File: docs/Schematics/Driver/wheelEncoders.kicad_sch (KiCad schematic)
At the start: 6 parts

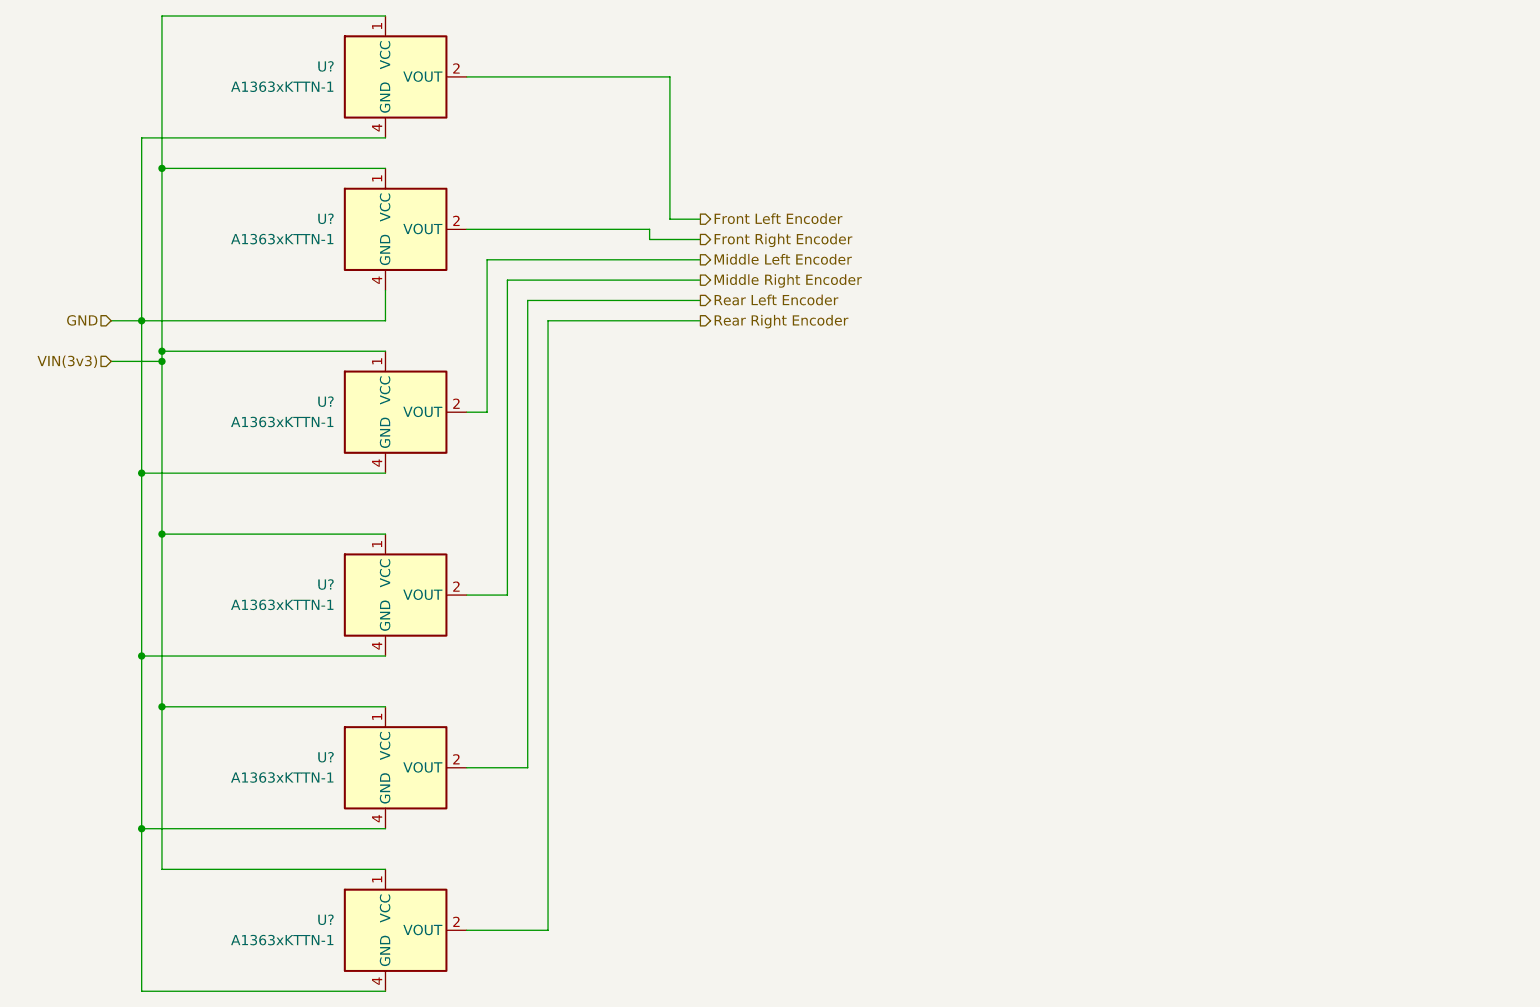
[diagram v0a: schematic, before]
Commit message: First scematic design for the card
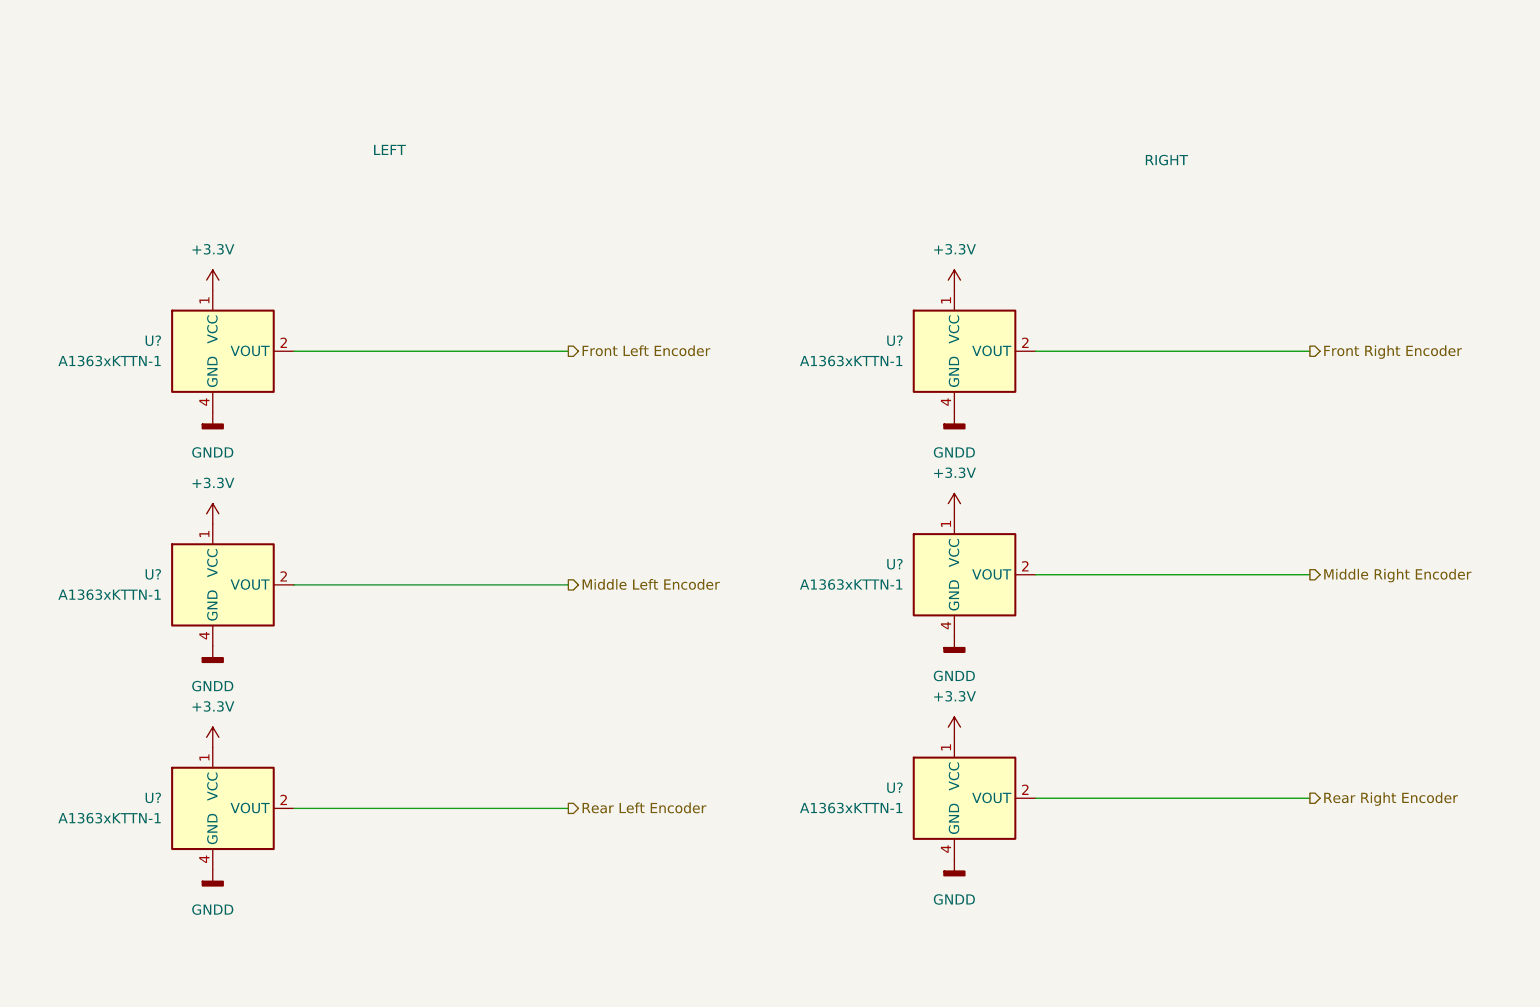
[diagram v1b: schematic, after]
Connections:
- net GND renamed GNDD
- net VIN(3v3) renamed +3.3V
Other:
- note added: "LEFT"
- note added: "RIGHT"
- company: (none) -> HiQ
- title: (none) -> Arty Z7 IO expander card
- moved on the sheet: U?

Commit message: Added footprints and a symbol for the level shifters
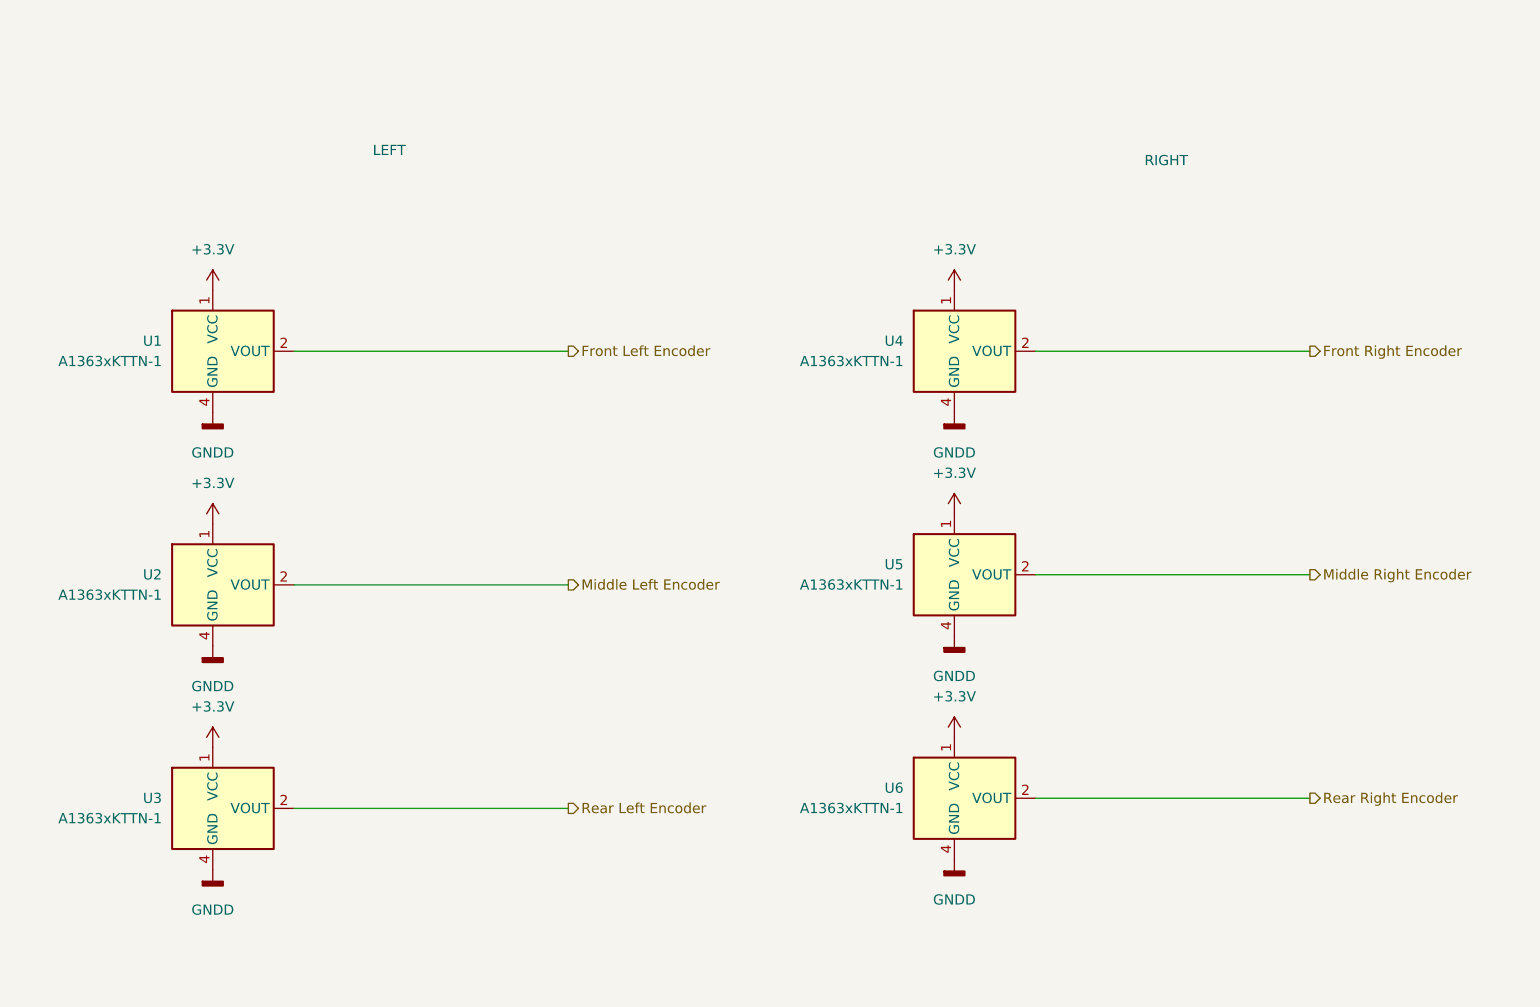
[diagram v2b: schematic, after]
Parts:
- gave numbers to parts that had none: 6
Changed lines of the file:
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@@
   (symbol (lib_id "Sensor_Current:A1363xKTTN-1") (at 87.63 92.71 0) (unit 1)
     (in_bom yes) (on_board yes) (fields_autoplaced)
-    (property "Reference" "U?" (id 0) (at 81.28 91.4399 0)
+    (property "Reference" "U2" (id 0) (at 81.28 91.4399 0)
       (effects (font (size 1.27 1.27)) (justify right))
     )
@@
   (symbol (lib_id "power:GNDD") (at 180.34 71.12 0) (unit 1)
     (in_bom yes) (on_board yes) (fields_autoplaced)
-    (property "Reference" "#PWR?" (id 0) (at 180.34 77.47 0)
+    (property "Reference" "#PWR043" (id 0) (at 180.34 77.47 0)
       (effects (font (size 1.27 1.27)) hide)
     )
@@
   (symbol (lib_id "power:GNDD") (at 87.63 100.33 0) (unit 1)
     (in_bom yes) (on_board yes) (fields_autoplaced)
-    (property "Reference" "#PWR?" (id 0) (at 87.63 106.68 0)
+    (property "Reference" "#PWR039" (id 0) (at 87.63 106.68 0)
       (effects (font (size 1.27 1.27)) hide)
     )
@@
   (symbol (lib_id "power:GNDD") (at 180.34 127 0) (unit 1)
     (in_bom yes) (on_board yes) (fields_autoplaced)
-    (property "Reference" "#PWR?" (id 0) (at 180.34 133.35 0)
+    (property "Reference" "#PWR047" (id 0) (at 180.34 133.35 0)
       (effects (font (size 1.27 1.27)) hide)
     )
@@
   (symbol (lib_id "Sensor_Current:A1363xKTTN-1") (at 87.63 120.65 0) (unit 1)
     (in_bom yes) (on_board yes) (fields_autoplaced)
-    (property "Reference" "U?" (id 0) (at 81.28 119.3799 0)
+    (property "Reference" "U3" (id 0) (at 81.28 119.3799 0)
       (effects (font (size 1.27 1.27)) (justify right))
     )
@@
   (symbol (lib_id "power:+3.3V") (at 87.63 113.03 0) (unit 1)
     (in_bom yes) (on_board yes) (fields_autoplaced)
-    (property "Reference" "#PWR?" (id 0) (at 87.63 116.84 0)
+    (property "Reference" "#PWR040" (id 0) (at 87.63 116.84 0)
       (effects (font (size 1.27 1.27)) hide)
     )
@@
   (symbol (lib_id "power:+3.3V") (at 87.63 55.88 0) (unit 1)
     (in_bom yes) (on_board yes) (fields_autoplaced)
-    (property "Reference" "#PWR?" (id 0) (at 87.63 59.69 0)
+    (property "Reference" "#PWR036" (id 0) (at 87.63 59.69 0)
       (effects (font (size 1.27 1.27)) hide)
     )
@@
   (symbol (lib_id "Sensor_Current:A1363xKTTN-1") (at 180.34 63.5 0) (unit 1)
     (in_bom yes) (on_board yes) (fields_autoplaced)
-    (property "Reference" "U?" (id 0) (at 173.99 62.2299 0)
+    (property "Reference" "U4" (id 0) (at 173.99 62.2299 0)
       (effects (font (size 1.27 1.27)) (justify right))
     )
@@
   (symbol (lib_id "power:+3.3V") (at 180.34 111.76 0) (unit 1)
     (in_bom yes) (on_board yes) (fields_autoplaced)
-    (property "Reference" "#PWR?" (id 0) (at 180.34 115.57 0)
+    (property "Reference" "#PWR046" (id 0) (at 180.34 115.57 0)
       (effects (font (size 1.27 1.27)) hide)
     )
@@
   (symbol (lib_id "power:+3.3V") (at 87.63 85.09 0) (unit 1)
     (in_bom yes) (on_board yes) (fields_autoplaced)
-    (property "Reference" "#PWR?" (id 0) (at 87.63 88.9 0)
+    (property "Reference" "#PWR038" (id 0) (at 87.63 88.9 0)
       (effects (font (size 1.27 1.27)) hide)
     )
@@
   (symbol (lib_id "power:GNDD") (at 180.34 99.06 0) (unit 1)
     (in_bom yes) (on_board yes) (fields_autoplaced)
-    (property "Reference" "#PWR?" (id 0) (at 180.34 105.41 0)
+    (property "Reference" "#PWR045" (id 0) (at 180.34 105.41 0)
       (effects (font (size 1.27 1.27)) hide)
     )
@@
   (symbol (lib_id "power:GNDD") (at 87.63 128.27 0) (unit 1)
     (in_bom yes) (on_board yes) (fields_autoplaced)
-    (property "Reference" "#PWR?" (id 0) (at 87.63 134.62 0)
+    (property "Reference" "#PWR041" (id 0) (at 87.63 134.62 0)
       (effects (font (size 1.27 1.27)) hide)
     )
@@
   (symbol (lib_id "Sensor_Current:A1363xKTTN-1") (at 87.63 63.5 0) (unit 1)
     (in_bom yes) (on_board yes) (fields_autoplaced)
-    (property "Reference" "U?" (id 0) (at 81.28 62.2299 0)
+    (property "Reference" "U1" (id 0) (at 81.28 62.2299 0)
       (effects (font (size 1.27 1.27)) (justify right))
     )
@@
   (symbol (lib_id "Sensor_Current:A1363xKTTN-1") (at 180.34 119.38 0) (unit 1)
     (in_bom yes) (on_board yes) (fields_autoplaced)
-    (property "Reference" "U?" (id 0) (at 173.99 118.1099 0)
+    (property "Reference" "U6" (id 0) (at 173.99 118.1099 0)
       (effects (font (size 1.27 1.27)) (justify right))
     )
@@
   (symbol (lib_id "power:+3.3V") (at 180.34 55.88 0) (unit 1)
     (in_bom yes) (on_board yes) (fields_autoplaced)
-    (property "Reference" "#PWR?" (id 0) (at 180.34 59.69 0)
+    (property "Reference" "#PWR042" (id 0) (at 180.34 59.69 0)
       (effects (font (size 1.27 1.27)) hide)
     )
@@
   (symbol (lib_id "power:+3.3V") (at 180.34 83.82 0) (unit 1)
     (in_bom yes) (on_board yes) (fields_autoplaced)
-    (property "Reference" "#PWR?" (id 0) (at 180.34 87.63 0)
+    (property "Reference" "#PWR044" (id 0) (at 180.34 87.63 0)
       (effects (font (size 1.27 1.27)) hide)
     )
@@
   (symbol (lib_id "power:GNDD") (at 87.63 71.12 0) (unit 1)
     (in_bom yes) (on_board yes) (fields_autoplaced)
-    (property "Reference" "#PWR?" (id 0) (at 87.63 77.47 0)
+    (property "Reference" "#PWR037" (id 0) (at 87.63 77.47 0)
       (effects (font (size 1.27 1.27)) hide)
     )
@@
   (symbol (lib_id "Sensor_Current:A1363xKTTN-1") (at 180.34 91.44 0) (unit 1)
     (in_bom yes) (on_board yes) (fields_autoplaced)
-    (property "Reference" "U?" (id 0) (at 173.99 90.1699 0)
-      (effects (font (size 1.27 1.27)) (justify right))
-    )
+    (property "Reference" "U5" (id 0) (at 173.99 90.1699 0)
+      (effects (font (size 1.27 1.27)) (justify right))
+    )

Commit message: Added caps and changed the connection from the motor sensors to plints
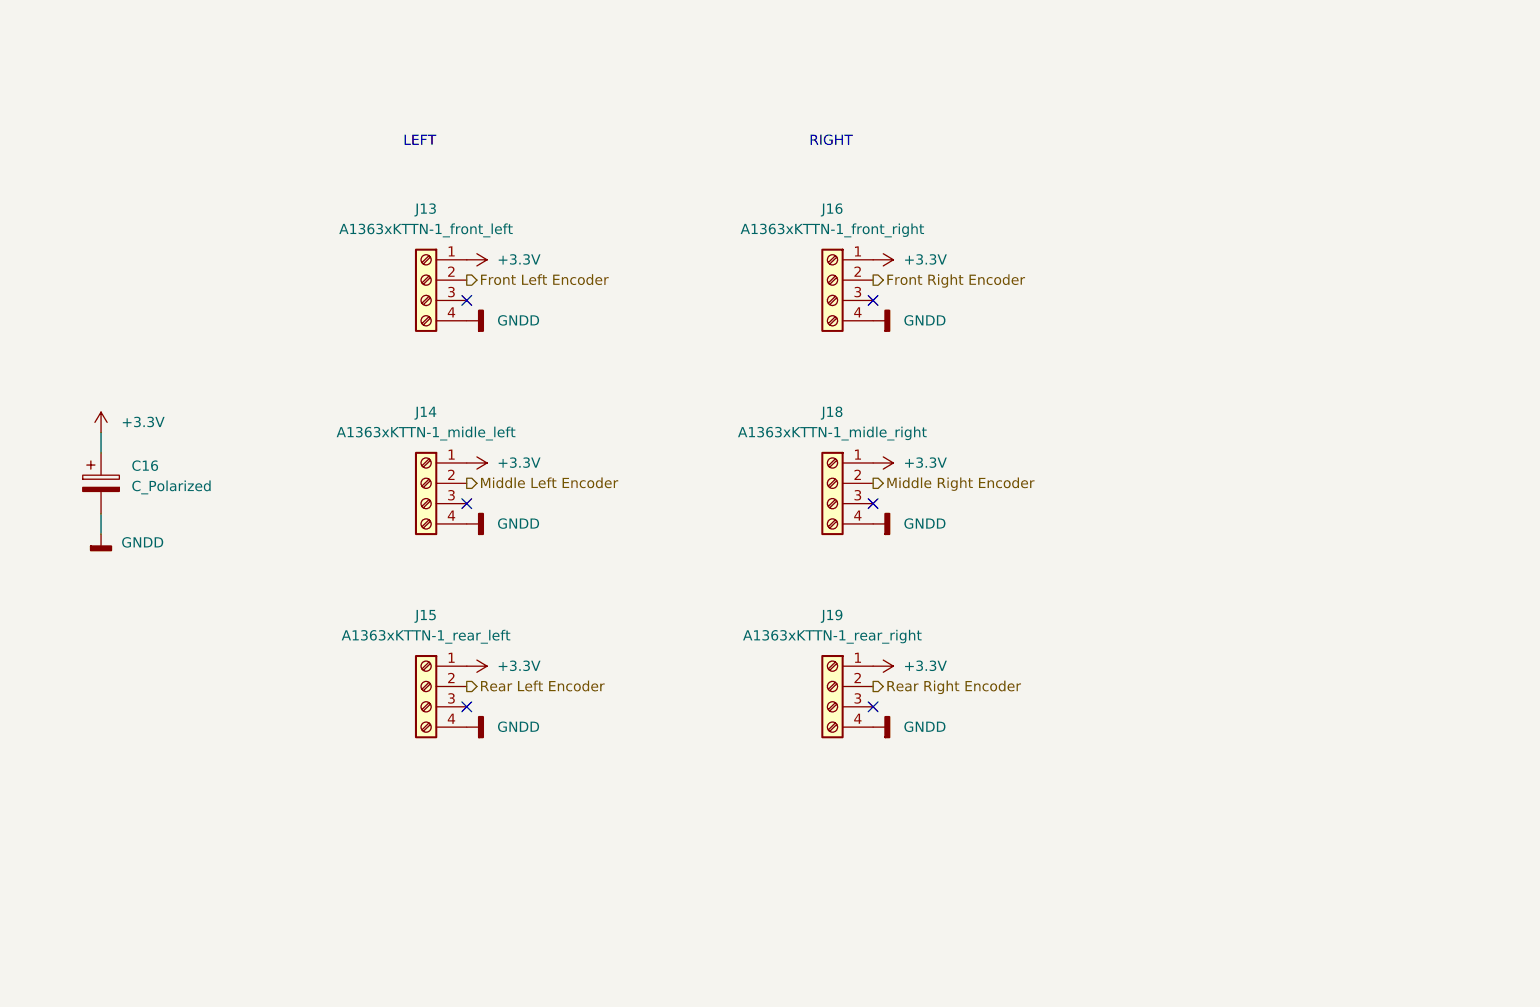
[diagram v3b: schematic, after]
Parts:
- removed U1, U2, U3, U4, U5, U6: A1363xKTTN-1, Sensor_Current:Allegro_SIP-4, symbol Sensor_Current:A1363xKTTN-1
- added C16: C_Polarized, Capacitor_THT:CP_Radial_D8.0mm_P3.80mm, symbol Device:C_Polarized
- added J13: A1363xKTTN-1_front_left, Connector_PinHeader_2.54mm:PinHeader_1x04_P2.54mm_Vertical, symbol Connector:Screw_Terminal_01x04
- added J14: A1363xKTTN-1_midle_left, Connector_PinHeader_2.54mm:PinHeader_1x04_P2.54mm_Vertical, symbol Connector:Screw_Terminal_01x04
- added J15: A1363xKTTN-1_rear_left, Connector_PinHeader_2.54mm:PinHeader_1x04_P2.54mm_Vertical, symbol Connector:Screw_Terminal_01x04
- added J16: A1363xKTTN-1_front_right, Connector_PinHeader_2.54mm:PinHeader_1x04_P2.54mm_Vertical, symbol Connector:Screw_Terminal_01x04
- added J18: A1363xKTTN-1_midle_right, Connector_PinHeader_2.54mm:PinHeader_1x04_P2.54mm_Vertical, symbol Connector:Screw_Terminal_01x04
- added J19: A1363xKTTN-1_rear_right, Connector_PinHeader_2.54mm:PinHeader_1x04_P2.54mm_Vertical, symbol Connector:Screw_Terminal_01x04
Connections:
- net +3.3V: now also C16.1, J13.1 (Pin_1), J14.1 (Pin_1), J15.1 (Pin_1), J16.1 (Pin_1), J18.1 (Pin_1), J19.1 (Pin_1)
- net Front Left Encoder: now also J13.2 (Pin_2)
- net Front Right Encoder: now also J16.2 (Pin_2)
- net GNDD: now also C16.2, J13.4 (Pin_4), J14.4 (Pin_4), J15.4 (Pin_4), J16.4 (Pin_4), J18.4 (Pin_4), J19.4 (Pin_4)
- net Middle Left Encoder: now also J14.2 (Pin_2)
- net Middle Right Encoder: now also J18.2 (Pin_2)
- net Rear Left Encoder: now also J15.2 (Pin_2)
- net Rear Right Encoder: now also J19.2 (Pin_2)
- no-connect marks 0 -> 6

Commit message: Started routing the pcb.
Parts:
- C16: footprint Capacitor_THT:CP_Radial_D8.0mm_P3.80mm -> Capacitor_SMD:C_0805_2012Metric_Pad1.18x1.45mm_HandSolder
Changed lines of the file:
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@@
       (effects (font (size 1.27 1.27)) (justify left))
     )
-    (property "Footprint" "Capacitor_THT:CP_Radial_D8.0mm_P3.80mm" (id 2) (at 74.6252 83.82 0)
+    (property "Footprint" "Capacitor_SMD:C_0805_2012Metric_Pad1.18x1.45mm_HandSolder" (id 2) (at 74.6252 83.82 0)
       (effects (font (size 1.27 1.27)) hide)
     )

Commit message: First version of the routed board is done
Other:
- title: Arty Z7 IO expander card -> Arty Z7 IO Board
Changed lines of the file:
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@@
   (paper "A4")
   (title_block
-    (title "Arty Z7 IO expander card")
+    (title "Arty Z7 IO Board")
     (date "2022-12-24")
-    (rev "0.1")
+    (rev "${VER}")
     (company "HiQ")
   )
